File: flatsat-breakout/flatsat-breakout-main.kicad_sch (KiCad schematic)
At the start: 5 parts, among them J1 SFM-120-02-L-DH-TR, J2 61204021621, J3 61204021621, J4 68000-227HLF, J5 Conn_02x08_Odd_Even

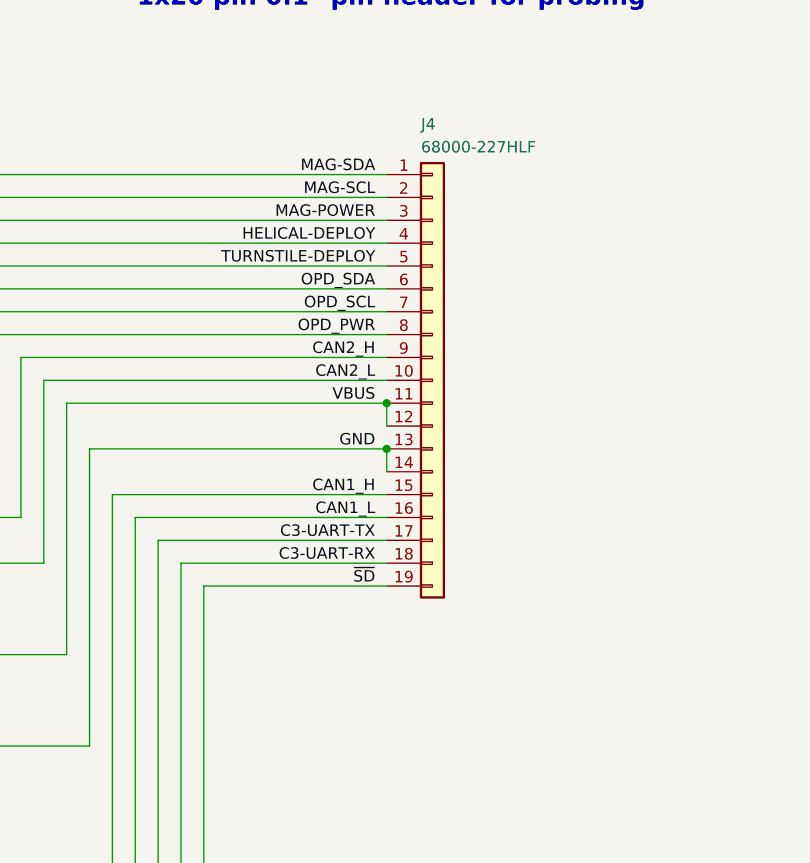
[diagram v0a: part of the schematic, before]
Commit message: Update flatsat-breakout schematic
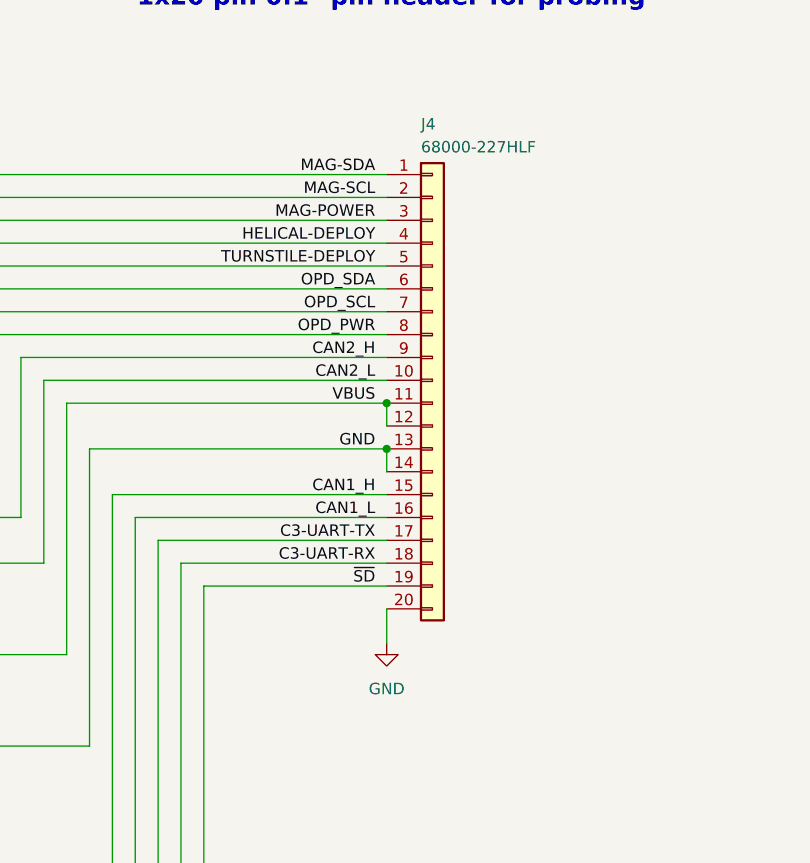
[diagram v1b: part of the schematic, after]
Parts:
- J2, J3: footprint (none) -> Connector_IDC:IDC-Header_2x20_P2.54mm_Vertical
- J4: footprint Connector_PinHeader_2.54mm:PinHeader_1x27_P2.54mm_Vertical -> Connector_PinHeader_2.54mm:PinHeader_1x20_P2.54mm_Vertical; symbol Connector_Generic:Conn_01x19 -> Connector_Generic:Conn_01x20
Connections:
- net GND: now also J4.20 (Pin_20)
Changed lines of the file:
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@@
+	(wire
+		(pts
+			(xy 255.27 129.54) (xy 255.27 133.35)
+		)
+		(stroke
+			(width 0)
+			(type default)
+		)
+	)
 	(wire
 		(pts
@@
 	)
 	(symbol
+		(lib_id "power:GND")
+		(at 255.27 133.35 0)
+		(unit 1)
+		(exclude_from_sim no)
+		(in_bom yes)
+		(on_board yes)
+		(dnp no)
+		(fields_autoplaced yes)
+		(property "Reference" "#PWR07"
+			(at 255.27 139.7 0)
+			(effects
+				(font
+					(size 1.27 1.27)
+				)
+				(hide yes)
+			)
+		)
+		(property "Value" "GND"
+			(at 255.27 138.43 0)
+			(effects
+				(font
+					(size 1.27 1.27)
+				)
+			)
+		)
+		(property "Footprint" ""
+			(at 255.27 133.35 0)
+			(effects
+				(font
+					(size 1.27 1.27)
+				)
+				(hide yes)
+			)
+		)
+		(property "Datasheet" ""
+			(at 255.27 133.35 0)
+			(effects
+				(font
+					(size 1.27 1.27)
+				)
+				(hide yes)
+			)
+		)
+		(property "Description" "Power symbol creates a global label with name \"GND\" , ground"
+			(at 255.27 133.35 0)
+			(effects
+				(font
+					(size 1.27 1.27)
+				)
+				(hide yes)
+			)
+		)
+		(pin "1"
+		)
+		(instances
+			(project "flatsat-breakout-main"
+				(path "/1685d9f1-2e37-4073-a34f-2675ab2d0a11"
+					(reference "#PWR07")
+					(unit 1)
+				)
+			)
+		)
+	)
+	(symbol
 		(lib_id "Connector_Generic:Conn_01x40")
 		(at 176.53 127 0)
@@
 			)
 		)
-		(property "Footprint" ""
+		(property "Footprint" "Connector_IDC:IDC-Header_2x20_P2.54mm_Vertical"
 			(at 176.53 127 0)
 			(effects
@@
 	)
 	(symbol
-		(lib_id "Connector_Generic:Conn_01x19")
+		(lib_id "Connector_Generic:Conn_01x20")
 		(at 260.35 104.14 0)
 		(unit 1)
@@
 			)
 		)
-		(property "Footprint" "Connector_PinHeader_2.54mm:PinHeader_1x27_P2.54mm_Vertical"
+		(property "Footprint" "Connector_PinHeader_2.54mm:PinHeader_1x20_P2.54mm_Vertical"
 			(at 260.35 104.14 0)
 			(effects
@@
 			)
 		)
-		(property "Description" "Generic connector, single row, 01x19, script generated (kicad-library-utils/schlib/autogen/connector/)"
+		(property "Description" "Generic connector, single row, 01x20, script generated (kicad-library-utils/schlib/autogen/connector/)"
 			(at 260.35 104.14 0)
 			(effects
@@
 		)
 		(pin "9"
+		)
+		(pin "20"
 		)
 		(instances
@@
 			)
 		)
-		(property "Footprint" ""
+		(property "Footprint" "Connector_IDC:IDC-Header_2x20_P2.54mm_Vertical"
 			(at 130.81 127 0)
 			(effects
